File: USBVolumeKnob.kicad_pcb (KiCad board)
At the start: 2 copper layers, 56 x 60 mm, 25 parts, among them J1 Conn_01x10_Male, SW1 SW_Push, SW2 SW_Push, U1 PEC12R-4xxxF

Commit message: Added custom library components and 3D data
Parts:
- J1: footprint Connector_PinHeader_2.54mm:PinHeader_1x10_P2.54mm_Vertical -> USBVolumeKnob:PinHeader_1x10_P2.54mm_Vertical

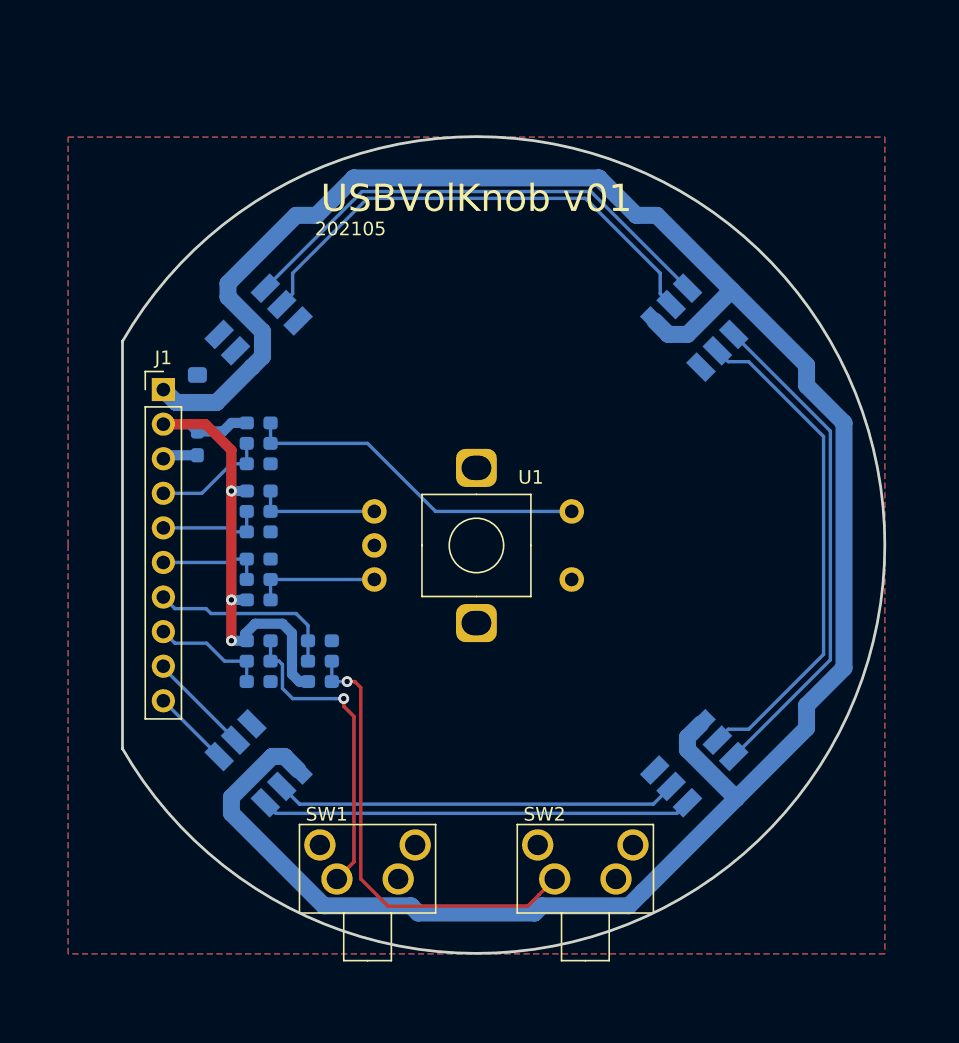
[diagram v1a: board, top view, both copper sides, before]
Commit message: Schamatic complete, component placement complete
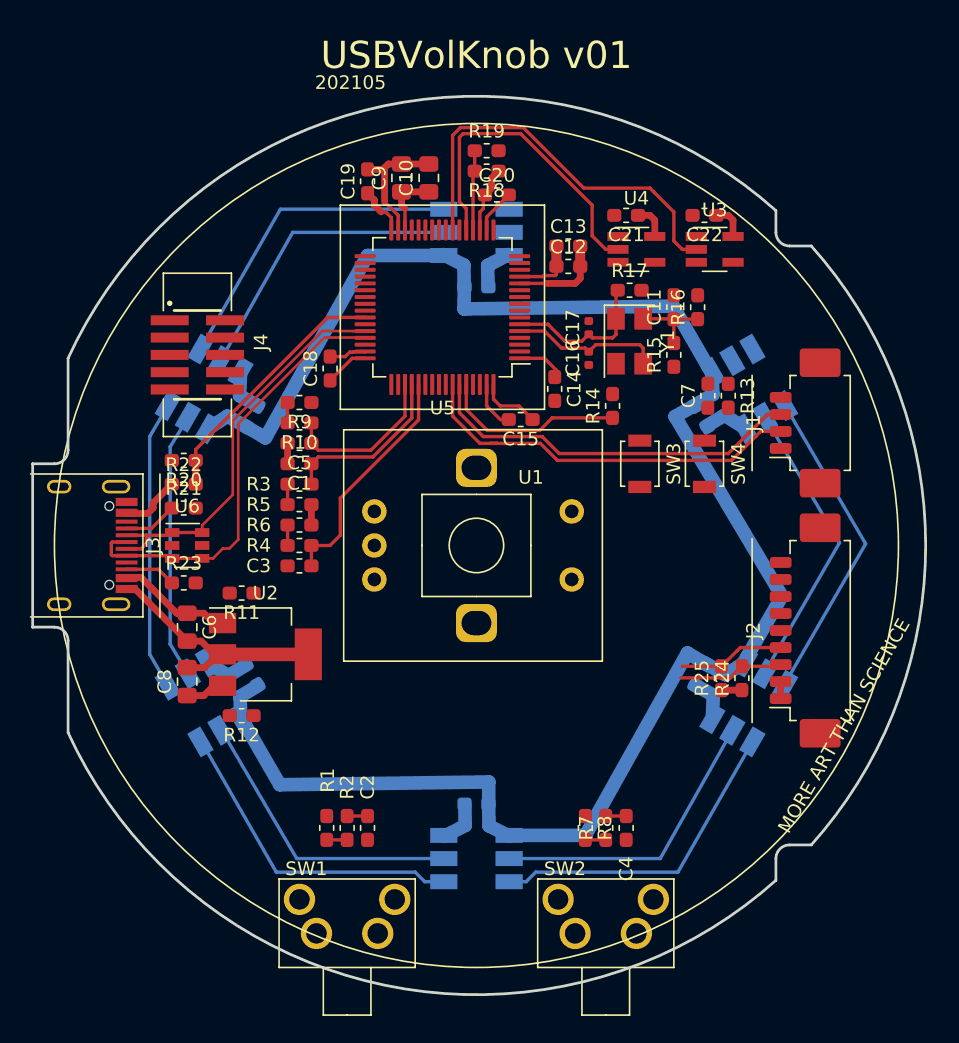
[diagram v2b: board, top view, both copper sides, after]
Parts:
- added C10: 2.2uF, Capacitor_SMD:C_0805_2012Metric_Pad1.15x1.40mm_HandSolder, F.Cu at (148.5, 75.0)
- added C11: 10nF, Capacitor_SMD:C_0603_1608Metric_Pad1.05x0.95mm_HandSolder, F.Cu at (166.5, 84.5)
- added C12: 1uF, Capacitor_SMD:C_0603_1608Metric_Pad1.05x0.95mm_HandSolder, F.Cu at (158.8, 81.5)
- added C13: 100nF, Capacitor_SMD:C_0603_1608Metric_Pad1.05x0.95mm_HandSolder, F.Cu at (158.8, 80.0)
- added C14: 100nF, Capacitor_SMD:C_0603_1608Metric_Pad1.05x0.95mm_HandSolder, F.Cu at (157.8, 90.5)
- added C15: 100nF, Capacitor_SMD:C_0603_1608Metric_Pad1.05x0.95mm_HandSolder, F.Cu at (155.2, 92.8)
- added C16: 9pF, Capacitor_SMD:C_0402_1005Metric, F.Cu at (160.2, 88.2)
- added C17: 9pF, Capacitor_SMD:C_0402_1005Metric, F.Cu at (160.2, 86.0)
- added C18: 100nF, Capacitor_SMD:C_0603_1608Metric_Pad1.05x0.95mm_HandSolder, F.Cu at (141.2, 89.0)
- added C19: 100nF, Capacitor_SMD:C_0603_1608Metric_Pad1.05x0.95mm_HandSolder, F.Cu at (144.0, 75.2)
- added C20: 100nF, Capacitor_SMD:C_0603_1608Metric_Pad1.05x0.95mm_HandSolder, F.Cu at (153.5, 76.2)
- added C21: 100nF, Capacitor_SMD:C_0603_1608Metric_Pad1.05x0.95mm_HandSolder, F.Cu at (163.0, 77.8)
- added C22: 100nF, Capacitor_SMD:C_0603_1608Metric_Pad1.05x0.95mm_HandSolder, F.Cu at (168.8, 77.8)
- added C23: 100nF, Capacitor_SMD:C_0603_1608Metric_Pad1.05x0.95mm_HandSolder, B.Cu at (152.0, 83.0)
- added C24: 100nF, Capacitor_SMD:C_0603_1608Metric_Pad1.05x0.95mm_HandSolder, B.Cu at (135.5, 92.5)
- added C25: 100nF, Capacitor_SMD:C_0603_1608Metric_Pad1.05x0.95mm_HandSolder, B.Cu at (135.5, 111.5)
- added C26: 100nF, Capacitor_SMD:C_0603_1608Metric_Pad1.05x0.95mm_HandSolder, B.Cu at (152.0, 121.0)
- added C27: 100nF, Capacitor_SMD:C_0603_1608Metric_Pad1.05x0.95mm_HandSolder, B.Cu at (168.5, 111.5)
- added C28: 100nF, Capacitor_SMD:C_0603_1608Metric_Pad1.05x0.95mm_HandSolder, B.Cu at (168.5, 92.5)
- added C8: 10uF, Capacitor_SMD:C_0805_2012Metric_Pad1.15x1.40mm_HandSolder, F.Cu at (130.8, 112.0)
- added C9: 2.2uF, Capacitor_SMD:C_0805_2012Metric_Pad1.15x1.40mm_HandSolder, F.Cu at (146.5, 75.0)
- added D5: SK9822, LED_SMD:LED_RGB_5050-6, B.Cu at (172.0, 113.5)
- added D6: SK9822, LED_SMD:LED_RGB_5050-6, B.Cu at (172.0, 90.5)
- added J2: Conn_01x09, Connector_Molex:Molex_PicoBlade_53261-0971_1x09-1MP_P1.25mm_Horizontal, F.Cu at (176.8, 108.2)
- added J3: USB_C_Receptacle_USB2.0, USBVolumeKnob:USB_C_Receptacle_Amphenol_12402012E212A, F.Cu at (118.8, 102.0)
- added J4: FTSH-105-01, USBVolumeKnob:SAMTEC_FTSH-105-XX-X-DV, F.Cu at (131.5, 88.0)
- added R11: 0, Resistor_SMD:R_0603_1608Metric_Pad1.05x0.95mm_HandSolder, F.Cu at (134.8, 105.5)
- added R12: 0, Resistor_SMD:R_0603_1608Metric_Pad1.05x0.95mm_HandSolder, F.Cu at (134.8, 114.5)
- added R13: 10k, Resistor_SMD:R_0603_1608Metric_Pad1.05x0.95mm_HandSolder, F.Cu at (170.5, 91.0)
- added R14: 10k, Resistor_SMD:R_0603_1608Metric_Pad1.05x0.95mm_HandSolder, F.Cu at (162.0, 91.8)
- added R15: 0, Resistor_SMD:R_0603_1608Metric_Pad1.05x0.95mm_HandSolder, F.Cu at (166.5, 88.0)
- added R16: 0, Resistor_SMD:R_0603_1608Metric_Pad1.05x0.95mm_HandSolder, F.Cu at (168.2, 84.5)
- added R17: 10k, Resistor_SMD:R_0603_1608Metric_Pad1.05x0.95mm_HandSolder, F.Cu at (163.2, 83.2)
- added R18: 10k, Resistor_SMD:R_0603_1608Metric_Pad1.05x0.95mm_HandSolder, F.Cu at (152.8, 74.5)
- added R19: 0, Resistor_SMD:R_0603_1608Metric_Pad1.05x0.95mm_HandSolder, F.Cu at (152.8, 73.0)
- added R20: 10k, Resistor_SMD:R_0603_1608Metric_Pad1.05x0.95mm_HandSolder, F.Cu at (130.5, 95.8)
- added R21: 5.1k, Resistor_SMD:R_0603_1608Metric_Pad1.05x0.95mm_HandSolder, F.Cu at (130.5, 99.2)
- added R22: 5.1k, Resistor_SMD:R_0603_1608Metric_Pad1.05x0.95mm_HandSolder, F.Cu at (130.5, 97.5)
- added R23: 5.1k, Resistor_SMD:R_0603_1608Metric_Pad1.05x0.95mm_HandSolder, F.Cu at (130.5, 104.8)
- added R24: 5.1k, Resistor_SMD:R_0603_1608Metric_Pad1.05x0.95mm_HandSolder, F.Cu at (171.5, 111.8)
- added R25: 5.1k, Resistor_SMD:R_0603_1608Metric_Pad1.05x0.95mm_HandSolder, F.Cu at (170.0, 111.8)
- added SW3: SW_Push, Button_Switch_SMD:SW_SPST_B3U-1000P, F.Cu at (164.0, 96.0)
- added SW4: SW_Push, Button_Switch_SMD:SW_SPST_B3U-1000P, F.Cu at (168.8, 96.0)
- added U2: LT1963AxST-3.3, Package_TO_SOT_SMD:SOT-223-3_TabPin2, F.Cu at (136.5, 110.0)
- added U3: SN74LV1T125, Package_TO_SOT_SMD:SOT-23-5_HandSoldering, F.Cu at (169.5, 80.2)
- added U4: SN74LV1T125, Package_TO_SOT_SMD:SOT-23-5_HandSoldering, F.Cu at (163.8, 80.2)
- added U5: STM32F401RCTx, Package_QFP:LQFP-64_10x10mm_P0.5mm, F.Cu at (149.5, 84.5)
- added U6: USBLC6-2SC6, Package_TO_SOT_SMD:SOT-23-6, F.Cu at (130.8, 102.0)
- added Y1: X1G004451000200, Crystal:Crystal_SMD_5032-4Pin_5.0x3.2mm, F.Cu at (163.2, 87.0)
- C1, C2, C3, C4, C5, R1, R10, R2, R3, R4, R5, R6, R7, R8, R9: moved to F.Cu
- C6: value 1uF -> 10uF; footprint Capacitor_SMD:C_0603_1608Metric_Pad1.05x0.95mm_HandSolder -> Capacitor_SMD:C_0805_2012Metric_Pad1.15x1.40mm_HandSolder; moved to F.Cu
- C7: value 4.7uF -> 100nF; footprint Capacitor_SMD:C_0805_2012Metric_Pad1.15x1.40mm_HandSolder -> Capacitor_SMD:C_0603_1608Metric_Pad1.05x0.95mm_HandSolder; moved to F.Cu
- J1: value Conn_01x10_Male -> Conn_01x04; footprint USBVolumeKnob:PinHeader_1x10_P2.54mm_Vertical -> Connector_Molex:Molex_PicoBlade_53261-0471_1x04-1MP_P1.25mm_Horizontal
- moved J1 47.8 mm to (176.8, 93.0), turned to 90 degrees
- moved D2 45.3 mm to (132.0, 90.5), turned to 240 degrees
- moved D3 45.3 mm to (132.0, 113.5), turned to 300 degrees
- moved D1 42.2 mm to (152.0, 79.0), turned to 180 degrees
- moved D4 42.2 mm to (152.0, 125.0), turned to 0 degrees
- moved C7 37.5 mm to (169.0, 91.0)
- moved C4 26.4 mm to (163.0, 122.8), turned to 270 degrees
- moved R7 24.3 mm to (161.5, 122.8), turned to 90 degrees
- moved R8 22.3 mm to (160.0, 122.7), turned to 270 degrees
- moved R2 14.6 mm to (141.0, 122.7), turned to 270 degrees
- moved R1 13.9 mm to (142.5, 122.8), turned to 90 degrees
- moved C6 13.5 mm to (130.8, 108.0)
- moved C2 13.4 mm to (144.0, 122.8), turned to 270 degrees
- moved R6 6.26 mm to (139.0, 100.5), turned to 180 degrees
- moved C1 5.83 mm to (139.0, 96.0), turned to 180 degrees
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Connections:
- C6 pad 1: +3V3 -> VBUS
- C7 pad 1: +5V -> /NRST
- D1 pad 1: /MOSI -> /MOSI_5V0
- D1 pad 2: /CLK -> /CLK_5V0
- D1 pad 4: +5V -> VDD
- D2 pad 4: +5V -> VDD
- D3 pad 4: +5V -> VDD
- D4 pad 4: +5V -> VDD
- J1 pad 1: +5V -> GND
- J1 pad 2: +3V3 -> /UART_TX
- J1 pad 3: GND -> /UART_RX
- J1 pad 4: /ENSW -> +3V3
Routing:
- net +5V: track 169.3 -> 0.00 mm
- net VDD: track 0.00 -> 137.8 mm
- net GND: track 2.61 -> 66.9 mm
- net /USB_D_P: track 0.00 -> 32.5 mm
- net Net-(R7-Pad1): track 33.8 -> 1.50 mm, vias 1 -> 0
- net /MOSI_3V3: track 0.00 -> 30.0 mm
- net /USB_D_N: track 0.00 -> 29.4 mm
- net /UART_TX: track 0.00 -> 29.2 mm
- net /UART_RX: track 0.00 -> 28.1 mm
- net Net-(R10-Pad2): track 25.7 -> 1.50 mm
- net Net-(D5-Pad6): track 0.00 -> 23.8 mm
- net Net-(D4-Pad6): track 0.00 -> 23.7 mm
- net /CLK_3V3: track 0.00 -> 23.6 mm
- net Net-(D4-Pad5): track 0.00 -> 21.9 mm
- net Net-(D5-Pad5): track 0.00 -> 21.9 mm
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- removed copper zone on B.Cu, net GND
- removed copper zone on F.Cu, net GND
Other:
- board size 56 x 60 mm -> 65.6 x 66 mm
- copper layers 2 -> 4
- board text added: "MORE ART THAN SCIENCE"

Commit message: Completed v02. Final schematic and layout.
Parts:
- added M1: MountingHole_2.2mm_M2_ISO14580, MountingHole:MountingHole_2.2mm_M2_ISO14580, F.Cu at (129.0, 83.0)
- added M2: MountingHole_2.2mm_M2_ISO14580, MountingHole:MountingHole_2.2mm_M2_ISO14580, F.Cu at (175.0, 83.0)
- added M3: MountingHole_2.2mm_M2_ISO14580, MountingHole:MountingHole_2.2mm_M2_ISO14580, F.Cu at (175.0, 121.0)
- added M4: MountingHole_2.2mm_M2_ISO14580, MountingHole:MountingHole_2.2mm_M2_ISO14580, F.Cu at (129.0, 121.0)
- moved J4 6.56 mm to (135.8, 83.0)
- moved C22 0.56 mm to (168.2, 77.5)
- moved U3 0.50 mm to (169.0, 80.2)
- moved C21 0.35 mm to (162.8, 77.5)
- moved U4 0.25 mm to (163.5, 80.2)
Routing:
- net +3V3: track 30.8 -> 203.6 mm, vias 0 -> 11
- net GND: track 66.9 -> 125.2 mm, vias 0 -> 71
- net /BTN1: track 1.50 -> 58.0 mm, vias 0 -> 2
- net /BTN0: track 1.50 -> 57.5 mm, vias 0 -> 2
- net /NRST: track 0.00 -> 52.5 mm, vias 0 -> 4
- net /PB14: track 0.00 -> 44.8 mm, vias 0 -> 2
- net /PB15: track 0.00 -> 44.8 mm, vias 0 -> 2
- net /PB13: track 0.00 -> 44.3 mm, vias 0 -> 2
- net /PB12: track 0.00 -> 43.2 mm, vias 0 -> 2
- net /PC09: track 7.75 -> 49.4 mm, vias 0 -> 2
- net /PA08: track 7.79 -> 47.3 mm, vias 0 -> 2
- net Net-(R10-Pad2): track 1.50 -> 28.8 mm, vias 0 -> 1
- net /SPI_EN: track 5.88 -> 30.3 mm, vias 0 -> 3
- net /SWO: track 0.00 -> 20.4 mm, vias 0 -> 2
- net /MOSI_5V0: track 0.00 -> 18.5 mm, vias 0 -> 1
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- added copper zone on In1.Cu, net +3V3
- added copper zone on B.Cu, net GND
- added copper zone on F.Cu, net GND
- added copper zone on In1.Cu, net GND
- added copper zone on In2.Cu, net GND
- added copper zone on B.Cu, net VDD
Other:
- board text added: "202110"
- board text added: "FAB NOTES: 1. FABRICATE PCB IN ACCORDANCE WITH THE CURRENT REVISION OF IPC-6012, CLASS 2. 2. MATERIAL SHALL BE FR4 Tg 180 C OR EQUIVALENT. 3. MATERIAL SHALL BE RoHS COMPLIANT, LEAD FREE, HALOGEN FREE. 4. ENIG PLATING PER CURRENT REVISION OF IPC-4552. 5. PLATING IN HOLES SHALL BE CONTINUOUS ELECTROLYTIC COPPER WITH 0.025 MM MINIMUM BARREL THICKNESS. FINISHED HOLE SIZE MEASURED AFTER PLATING. 6. SO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"
- board text added: "USBVolKnob v02"
- board text removed: "202105"
- board text removed: "USBVolKnob v01"
